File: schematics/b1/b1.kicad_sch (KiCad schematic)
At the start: 7 parts, among them SW6 SW_SPDT, U1 L7805, U8 AMS1117-3.3

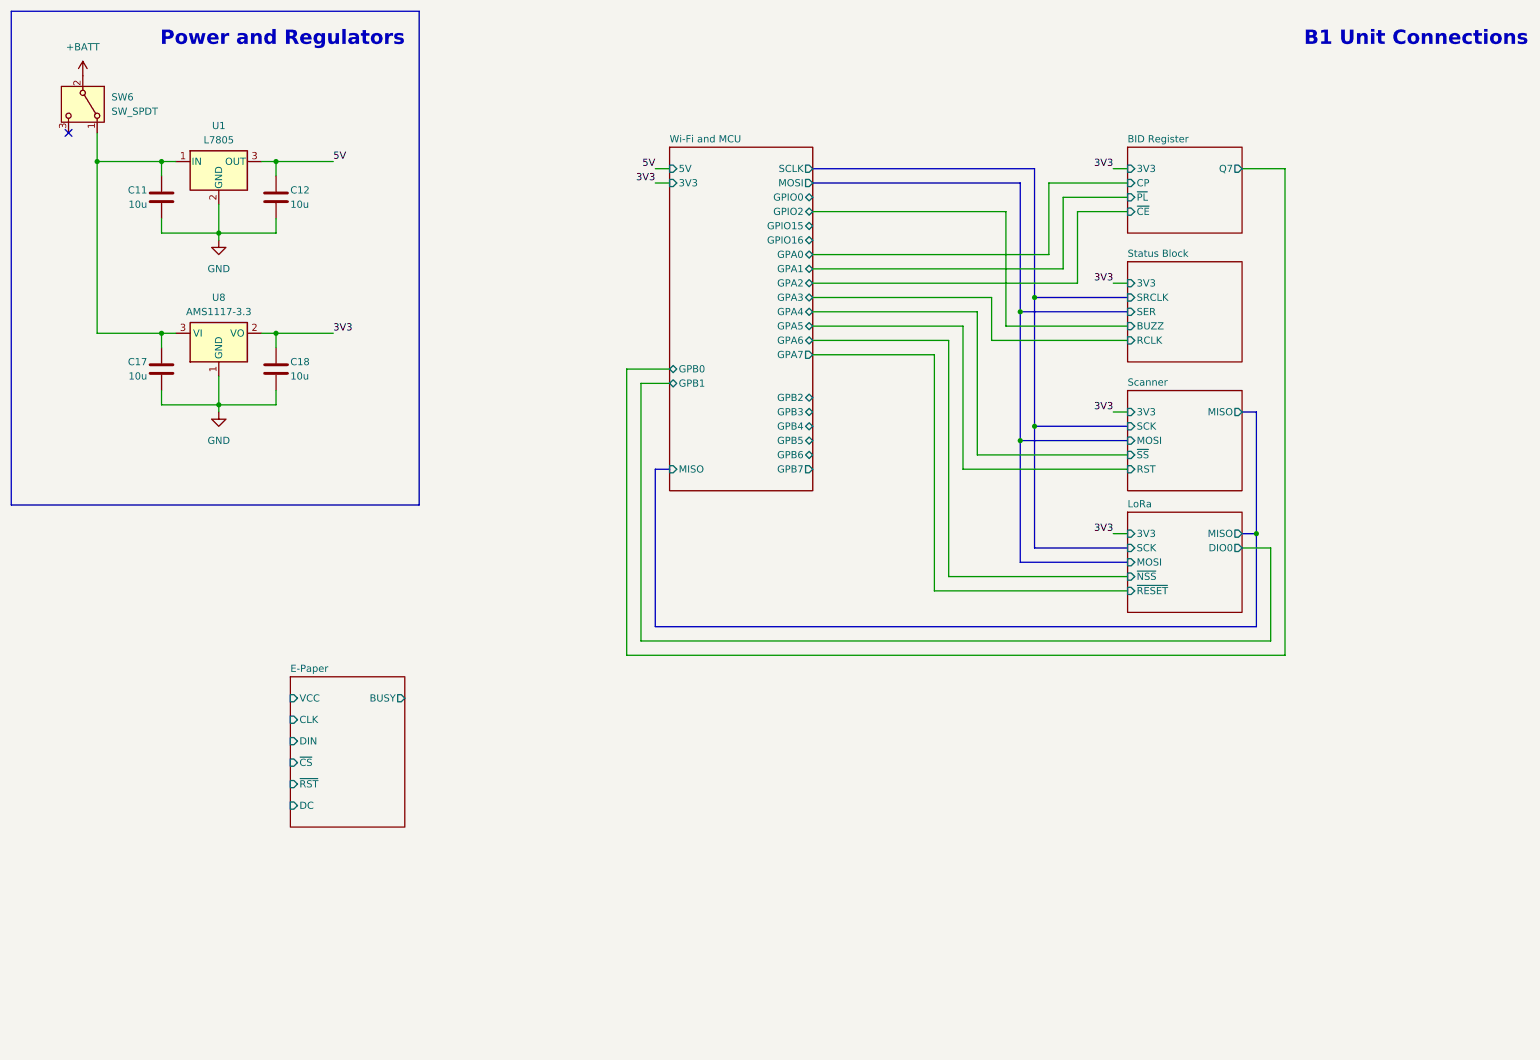
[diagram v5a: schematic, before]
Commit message: Increased capacitance and added some test points.
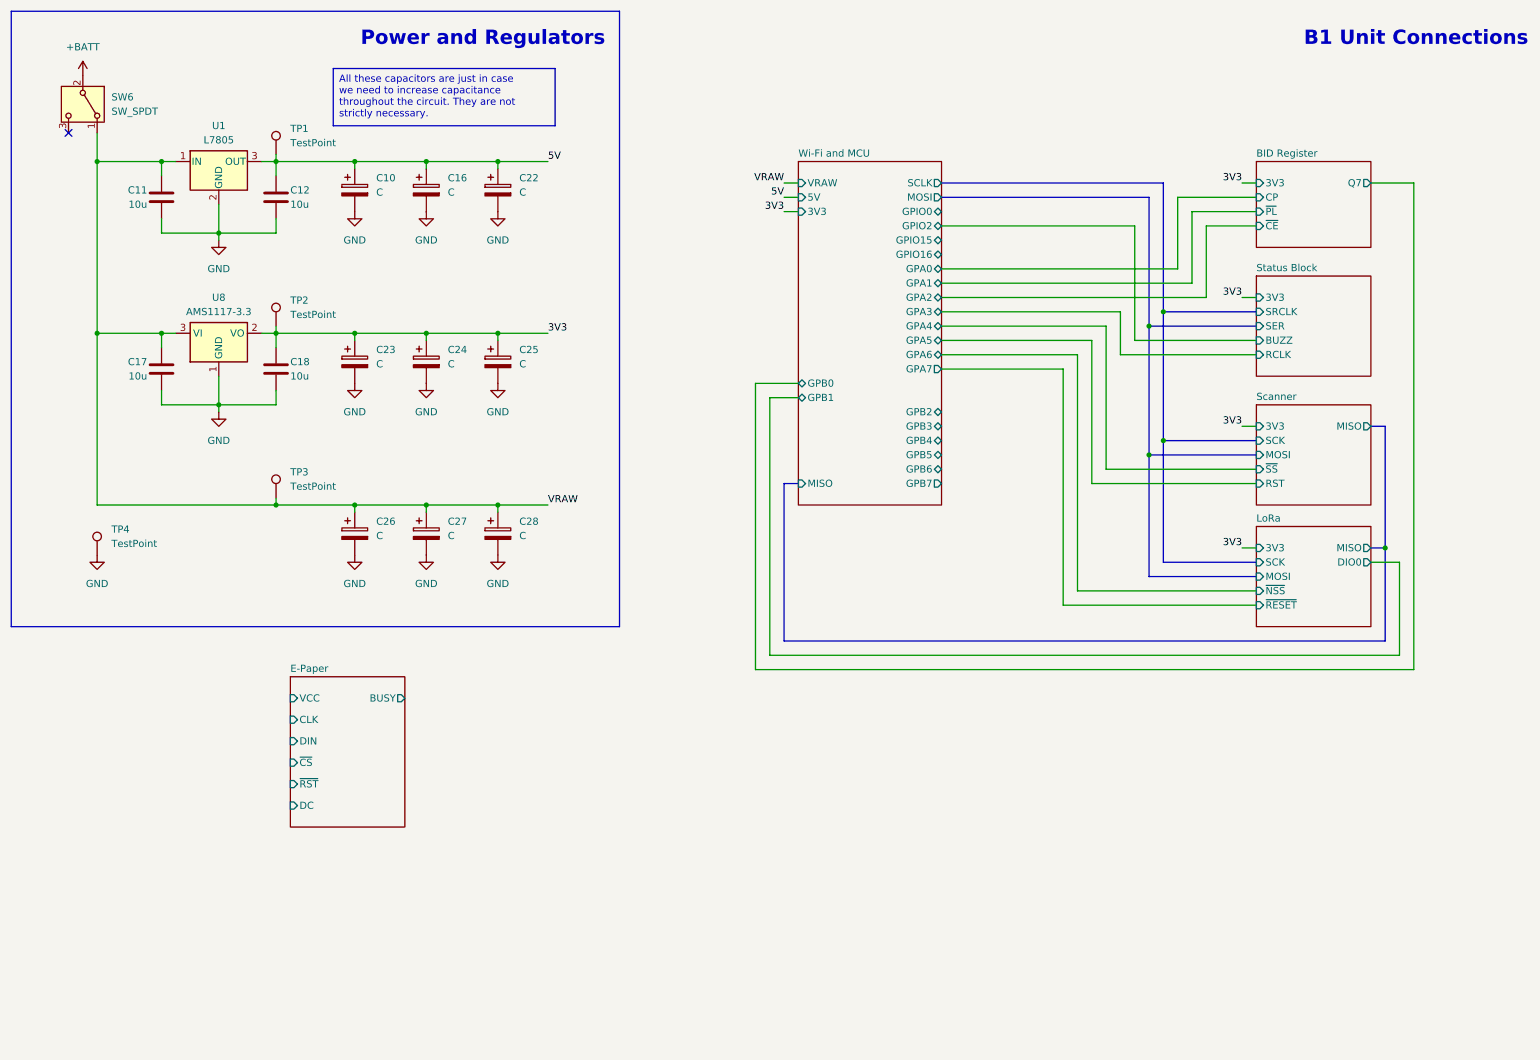
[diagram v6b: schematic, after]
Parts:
- added C10, C16, C22, C23, C24, C25, C26, C27, C28: C, symbol Device:C_Polarized
- added TP1, TP2, TP3, TP4: TestPoint, symbol Connector:TestPoint
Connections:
- net 3V3: now also C23.1, C24.1, C25.1, TP2.1
- net 5V: now also C10.1, C16.1, C22.1, TP1.1
- net GND: now also C10.2, C16.2, C22.2, C23.2, C24.2, C25.2, C26.2, C27.2, C28.2, TP4.1
- net VRAW: now reaches C11.1, C17.1, SW6.1 (A), U1.1 (IN), U8.3 (VI)
- net VRAW: now also C26.1, C27.1, C28.1, TP3.1
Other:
- sheet Wi-Fi and MCU ports: added VRAW; removed none

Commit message: Added a bunch of test points.
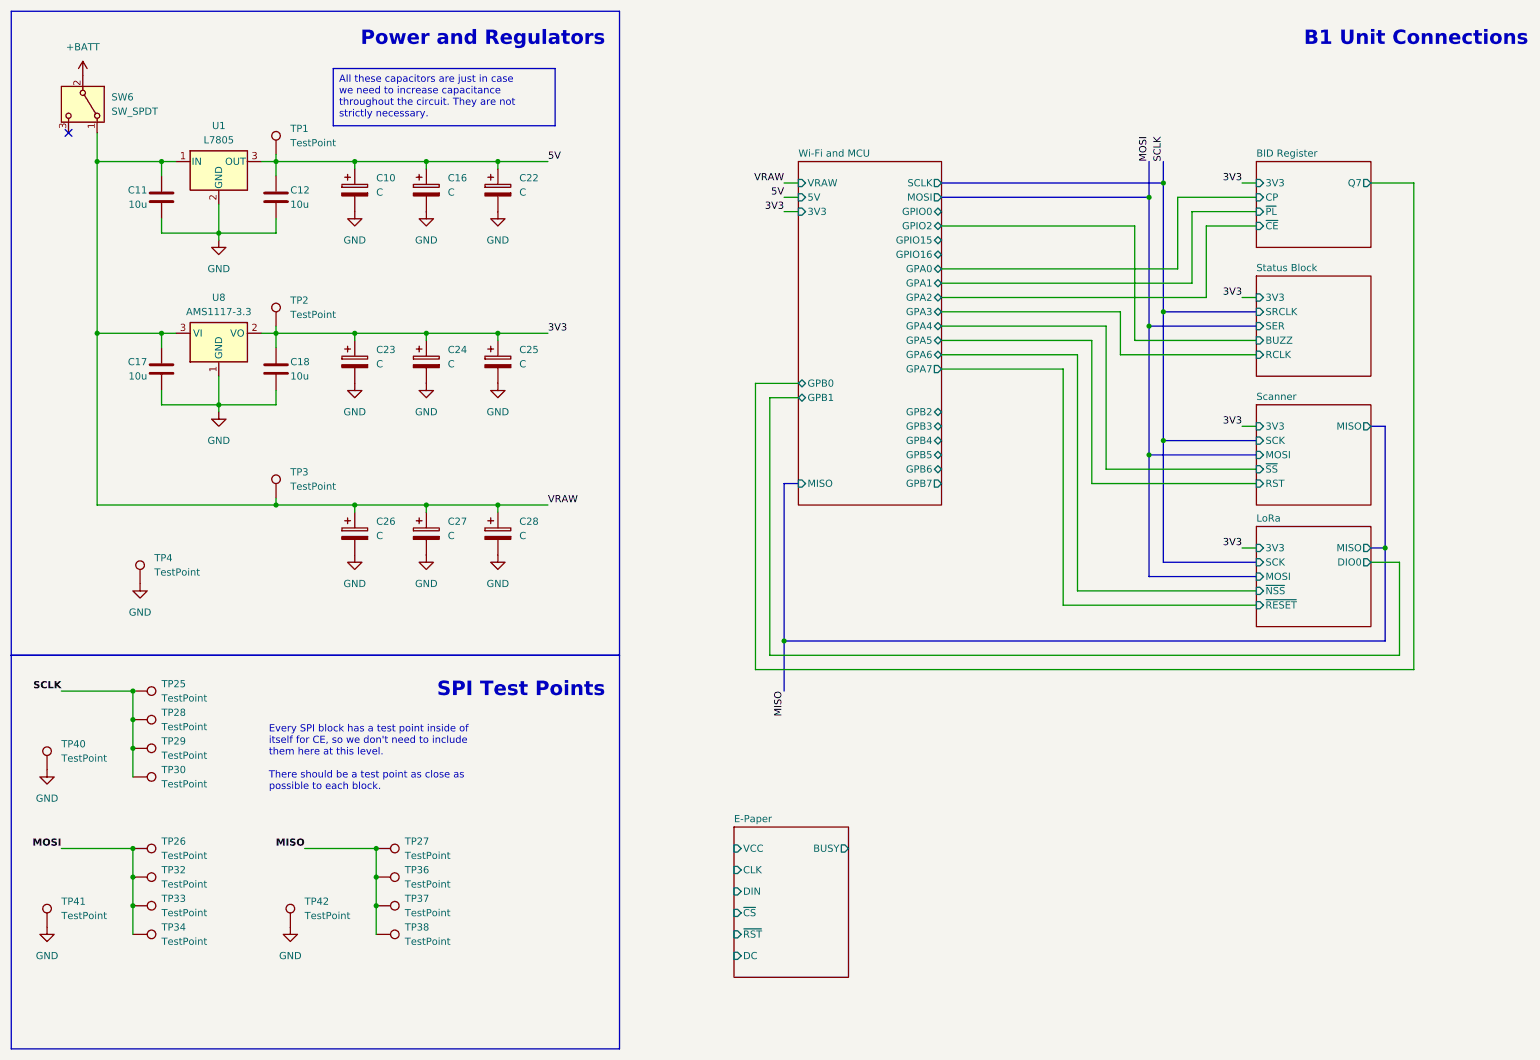
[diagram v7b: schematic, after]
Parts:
- added TP25, TP26, TP27, TP28, TP29, TP30, TP32, TP33, TP34, TP36, TP37, TP38, TP40, TP41, TP42: TestPoint, symbol Connector:TestPoint
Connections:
- net GND: now also TP40.1, TP41.1, TP42.1
- new net MISO: TP27.1, TP36.1, TP37.1, TP38.1
- new net MOSI: TP26.1, TP32.1, TP33.1, TP34.1
- new net SCLK: TP25.1, TP28.1, TP29.1, TP30.1
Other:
- note added: "Every SPI block has a test point inside of itself for CE, so we don't need to include them here at this level. There should be a test point as close as possible to each block."
- note added: "SPI Test Points"
- moved on the sheet: TP4
